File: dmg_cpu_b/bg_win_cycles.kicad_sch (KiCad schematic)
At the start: 68 parts

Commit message: Fixes based on review. + various other edits.
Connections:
- net CLK2: now also LEBO.1
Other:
- moved on the sheet: LYRY, MOCE
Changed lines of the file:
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@@
     (comment 1 "https://github.com/msinger/dmg-schematics")
   )
-  (junction (at 104.14 89.535) (diameter 0) (color 0 0 0 0)
+  (junction (at 104.14 85.725) (diameter 0) (color 0 0 0 0)
   )
   (junction (at 48.26 54.61) (diameter 0) (color 0 0 0 0)
@@
   (junction (at 153.035 253.365) (diameter 0) (color 0 0 0 0)
   )
+  (junction (at 81.28 71.755) (diameter 0) (color 0 0 0 0)
+  )
   (junction (at 183.515 255.905) (diameter 0) (color 0 0 0 0)
   )
@@
   (junction (at 76.2 76.835) (diameter 0) (color 0 0 0 0)
   )
-  (junction (at 48.26 89.535) (diameter 0) (color 0 0 0 0)
+  (junction (at 130.175 85.725) (diameter 0) (color 0 0 0 0)
   )
   (junction (at 262.89 150.495) (diameter 0) (color 0 0 0 0)
@@
   (junction (at 168.91 111.125) (diameter 0) (color 0 0 0 0)
   )
+  (junction (at 48.26 85.725) (diameter 0) (color 0 0 0 0)
+  )
   (junction (at 188.595 231.14) (diameter 0) (color 0 0 0 0)
   )
@@
   )
   (junction (at 297.815 227.33) (diameter 0) (color 0 0 0 0)
-  )
-  (junction (at 78.74 71.755) (diameter 0) (color 0 0 0 0)
   )
   (junction (at 343.535 214.63) (diameter 0) (color 0 0 0 0)
@@
     (stroke (width 0) (type default) (color 0 0 0 0))
   )
-  (wire (pts (xy 73.66 71.755) (xy 78.74 71.755))
+  (wire (pts (xy 73.66 71.755) (xy 81.28 71.755))
     (stroke (width 0) (type default) (color 0 0 0 0))
   )
@@
     (stroke (width 0) (type default) (color 0 0 0 0))
   )
+  (wire (pts (xy 130.175 85.725) (xy 130.175 89.535))
+    (stroke (width 0) (type default) (color 0 0 0 0))
+  )
   (wire (pts (xy 300.355 217.17) (xy 300.355 212.09))
     (stroke (width 0) (type default) (color 0 0 0 0))
@@
     (stroke (width 0) (type default) (color 0 0 0 0))
   )
-  (wire (pts (xy 27.94 95.25) (xy 104.14 95.25))
+  (wire (pts (xy 27.94 92.075) (xy 104.14 92.075))
     (stroke (width 0) (type default) (color 0 0 0 0))
   )
@@
     (stroke (width 0) (type default) (color 0 0 0 0))
   )
-  (wire (pts (xy 101.6 89.535) (xy 104.14 89.535))
+  (wire (pts (xy 101.6 85.725) (xy 104.14 85.725))
     (stroke (width 0) (type default) (color 0 0 0 0))
   )
@@
     (stroke (width 0) (type default) (color 0 0 0 0))
   )
-  (wire (pts (xy 83.82 32.385) (xy 83.82 86.995))
-    (stroke (width 0) (type default) (color 0 0 0 0))
-  )
-  (wire (pts (xy 48.26 74.295) (xy 48.26 89.535))
+  (wire (pts (xy 83.82 32.385) (xy 83.82 83.185))
+    (stroke (width 0) (type default) (color 0 0 0 0))
+  )
+  (wire (pts (xy 48.26 74.295) (xy 48.26 85.725))
     (stroke (width 0) (type default) (color 0 0 0 0))
   )
@@
     (stroke (width 0) (type default) (color 0 0 0 0))
   )
-  (wire (pts (xy 48.26 89.535) (xy 86.36 89.535))
+  (wire (pts (xy 48.26 85.725) (xy 86.36 85.725))
     (stroke (width 0) (type default) (color 0 0 0 0))
   )
@@
     (stroke (width 0) (type default) (color 0 0 0 0))
   )
-  (wire (pts (xy 83.82 86.995) (xy 86.36 86.995))
+  (wire (pts (xy 83.82 83.185) (xy 86.36 83.185))
     (stroke (width 0) (type default) (color 0 0 0 0))
   )
@@
     (stroke (width 0) (type default) (color 0 0 0 0))
   )
-  (wire (pts (xy 78.74 71.755) (xy 78.74 92.075))
+  (wire (pts (xy 81.28 71.755) (xy 81.28 88.265))
     (stroke (width 0) (type default) (color 0 0 0 0))
   )
@@
     (stroke (width 0) (type default) (color 0 0 0 0))
   )
-  (wire (pts (xy 27.94 74.295) (xy 27.94 95.25))
+  (wire (pts (xy 27.94 74.295) (xy 27.94 92.075))
     (stroke (width 0) (type default) (color 0 0 0 0))
   )
@@
     (stroke (width 0) (type default) (color 0 0 0 0))
   )
+  (wire (pts (xy 81.28 71.755) (xy 94.615 71.755))
+    (stroke (width 0) (type default) (color 0 0 0 0))
+  )
   (wire (pts (xy 302.26 133.985) (xy 304.8 133.985))
     (stroke (width 0) (type default) (color 0 0 0 0))
@@
     (stroke (width 0) (type default) (color 0 0 0 0))
   )
-  (wire (pts (xy 104.14 89.535) (xy 106.68 89.535))
+  (wire (pts (xy 104.14 85.725) (xy 106.68 85.725))
     (stroke (width 0) (type default) (color 0 0 0 0))
   )
@@
     (stroke (width 0) (type default) (color 0 0 0 0))
   )
-  (wire (pts (xy 130.175 80.01) (xy 130.175 89.535))
+  (wire (pts (xy 130.175 80.01) (xy 130.175 85.725))
     (stroke (width 0) (type default) (color 0 0 0 0))
   )
@@
     (stroke (width 0) (type default) (color 0 0 0 0))
   )
-  (wire (pts (xy 130.175 89.535) (xy 119.38 89.535))
+  (wire (pts (xy 130.175 85.725) (xy 119.38 85.725))
     (stroke (width 0) (type default) (color 0 0 0 0))
   )
@@
     (stroke (width 0) (type default) (color 0 0 0 0))
   )
-  (wire (pts (xy 104.14 89.535) (xy 104.14 95.25))
+  (wire (pts (xy 104.14 85.725) (xy 104.14 92.075))
     (stroke (width 0) (type default) (color 0 0 0 0))
   )
@@
     (stroke (width 0) (type default) (color 0 0 0 0))
   )
-  (wire (pts (xy 78.74 71.755) (xy 94.615 71.755))
-    (stroke (width 0) (type default) (color 0 0 0 0))
-  )
   (wire (pts (xy 53.34 74.295) (xy 48.26 74.295))
     (stroke (width 0) (type default) (color 0 0 0 0))
@@
     (stroke (width 0) (type default) (color 0 0 0 0))
   )
-  (wire (pts (xy 48.26 89.535) (xy 48.26 97.155))
+  (wire (pts (xy 48.26 85.725) (xy 48.26 97.155))
     (stroke (width 0) (type default) (color 0 0 0 0))
   )
@@
     (stroke (width 0) (type default) (color 0 0 0 0))
   )
-  (wire (pts (xy 78.74 92.075) (xy 86.36 92.075))
+  (wire (pts (xy 81.28 88.265) (xy 86.36 88.265))
     (stroke (width 0) (type default) (color 0 0 0 0))
   )
@@
   )
   (text "HORIZONTAL SYNC" (at 378.46 162.56 0)
+    (effects (font (size 1.27 1.27)) (justify left bottom))
+  )
+  (label "CLK2" (at 25.4 69.215 0)
     (effects (font (size 1.27 1.27)) (justify left bottom))
   )
@@
     (pin "2")
   )
-  (symbol (lib_id "DMG_CPU_Cells:NAND_3") (at 93.98 89.535 0) (unit 1)
-    (in_bom yes) (on_board yes) (fields_autoplaced)
-    (property "Reference" "MOCE" (id 0) (at 93.98 82.0252 0))
-    (property "Value" "NAND_3" (id 1) (at 93.98 84.5621 0))
-    (property "Footprint" "" (id 2) (at 93.98 89.535 0)
-      (effects (font (size 1.27 1.27)) hide)
-    )
-    (property "Datasheet" "http://iceboy.a-singer.de/doc/dmg_cells.html#nand3" (id 3) (at 93.98 97.155 0)
+  (symbol (lib_id "DMG_CPU_Cells:NAND_3") (at 93.98 85.725 0) (unit 1)
+    (in_bom yes) (on_board yes) (fields_autoplaced)
+    (property "Reference" "MOCE" (id 0) (at 93.98 78.2152 0))
+    (property "Value" "NAND_3" (id 1) (at 93.98 80.7521 0))
+    (property "Footprint" "" (id 2) (at 93.98 85.725 0)
+      (effects (font (size 1.27 1.27)) hide)
+    )
+    (property "Datasheet" "http://iceboy.a-singer.de/doc/dmg_cells.html#nand3" (id 3) (at 93.98 93.345 0)
       (effects (font (size 1.27 1.27)) hide)
     )
@@
     (pin "4")
   )
-  (symbol (lib_id "DMG_CPU_Cells:INVERTER_A") (at 113.03 89.535 0) (unit 1)
-    (in_bom yes) (on_board yes) (fields_autoplaced)
-    (property "Reference" "LYRY" (id 0) (at 113.03 82.0252 0))
-    (property "Value" "INVERTER_A" (id 1) (at 113.03 84.5621 0))
-    (property "Footprint" "" (id 2) (at 110.49 89.535 0)
-      (effects (font (size 1.27 1.27)) hide)
-    )
-    (property "Datasheet" "http://iceboy.a-singer.de/doc/dmg_cells.html#inv_a" (id 3) (at 114.3 97.155 0)
-      (effects (font (size 1.27 1.27)) hide)
-    )
+  (symbol (lib_id "DMG_CPU_Cells:INVERTER_A") (at 113.03 85.725 0) (unit 1)
+    (in_bom yes) (on_board yes) (fields_autoplaced)
+    (property "Reference" "LYRY" (id 0) (at 113.03 78.2152 0))
+    (property "Value" "INVERTER_A" (id 1) (at 113.03 80.7521 0))
+    (property "Footprint" "" (id 2) (at 110.49 85.725 0)
+      (effects (font (size 1.27 1.27)) hide)
+    )
+    (property "Datasheet" "http://iceboy.a-singer.de/doc/dmg_cells.html#inv_a" (id 3) (at 114.3 93.345 0)
+      (effects (font (size 1.27 1.27)) hide)
+    )

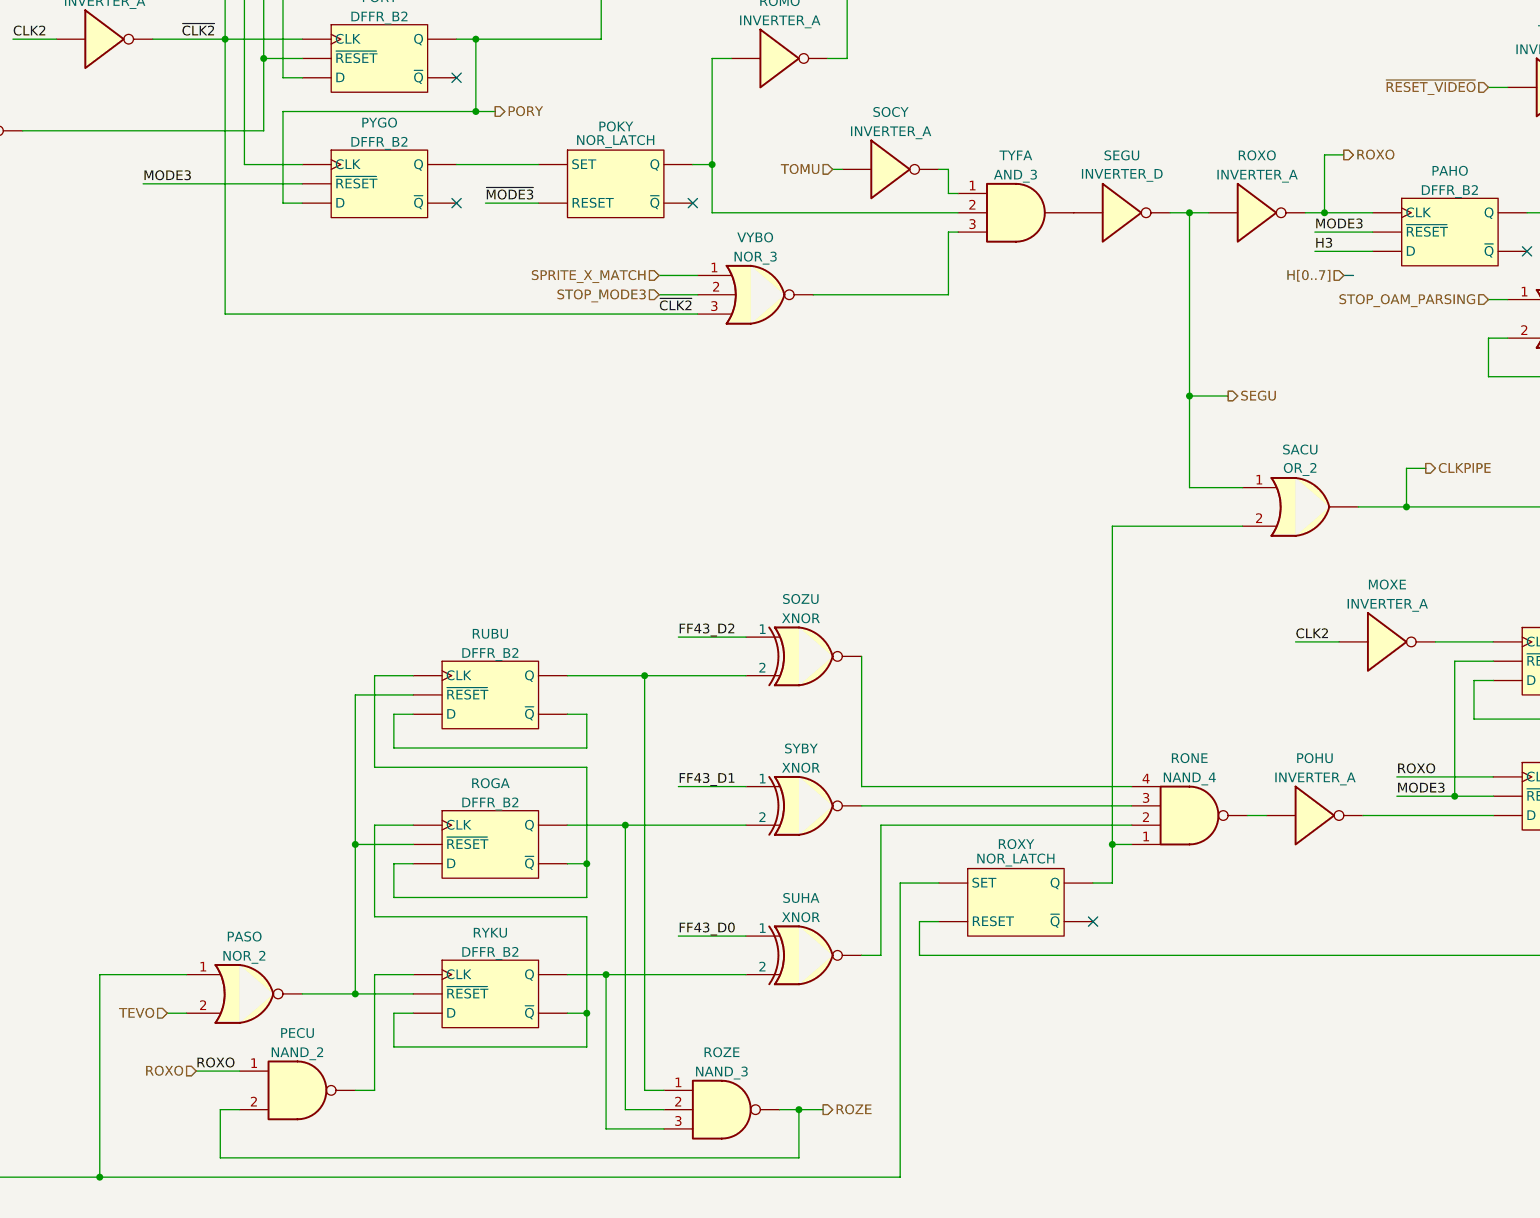
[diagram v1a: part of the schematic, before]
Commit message: Changes made based on review. PPU hierarchcal sheet work started.
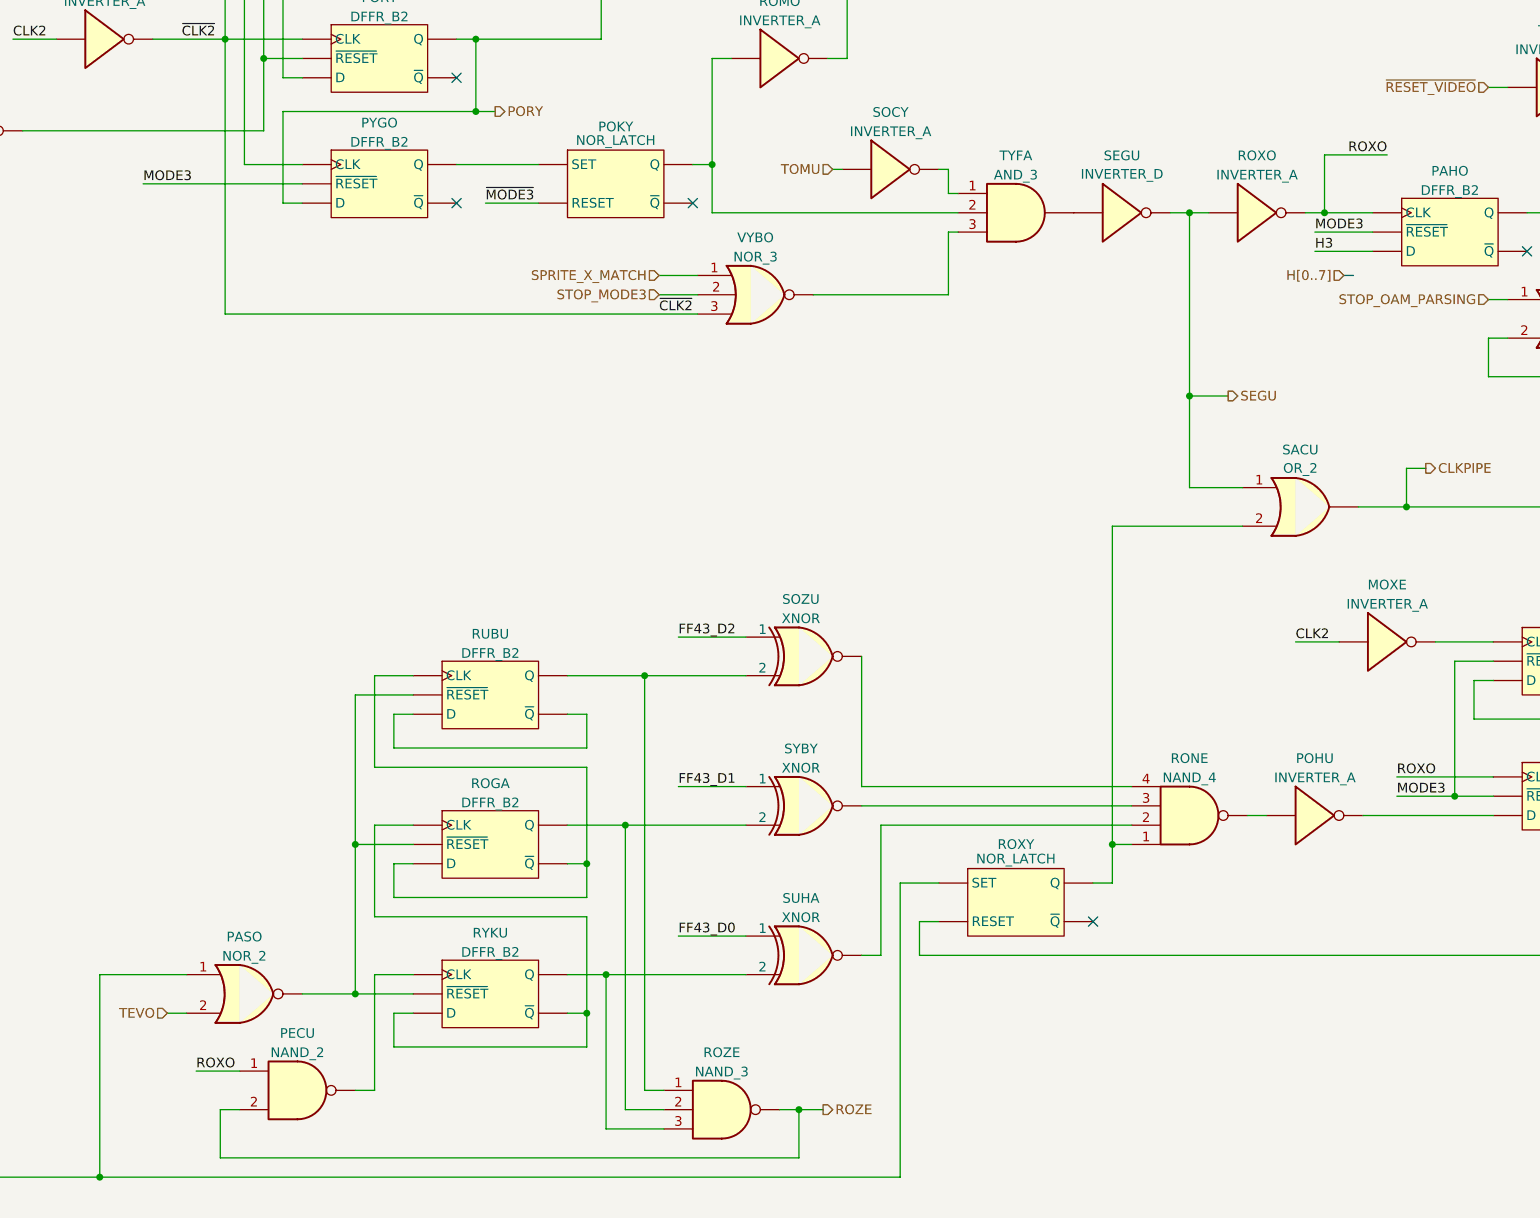
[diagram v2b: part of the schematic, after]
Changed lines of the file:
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@@
     (stroke (width 0) (type default) (color 0 0 0 0))
   )
-  (wire (pts (xy 280.67 142.875) (xy 283.21 142.875))
+  (wire (pts (xy 280.67 142.875) (xy 288.925 142.875))
     (stroke (width 0) (type default) (color 0 0 0 0))
   )
@@
     (effects (font (size 1.27 1.27)) (justify left bottom))
   )
+  (label "ROXO" (at 288.925 142.875 180)
+    (effects (font (size 1.27 1.27)) (justify right bottom))
+  )
   (label "ROXO" (at 290.195 224.79 0)
     (effects (font (size 1.27 1.27)) (justify left bottom))
@@
     (effects (font (size 1.27 1.27)) (justify left))
   )
-  (hierarchical_label "ROXO" (shape input) (at 132.08 263.525 180)
-    (effects (font (size 1.27 1.27)) (justify right))
-  )
   (hierarchical_label "MOFU" (shape output) (at 207.01 61.595 0)
     (effects (font (size 1.27 1.27)) (justify left))
@@
     (effects (font (size 1.27 1.27)) (justify left))
   )
-  (hierarchical_label "ROXO" (shape output) (at 283.21 142.875 0)
-    (effects (font (size 1.27 1.27)) (justify left))
-  )

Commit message: PPU hierarchical page progress. Elements moved out of window sheet to be includes in BG and WIN cycles sheet
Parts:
- added MEHE, NOCU, NYFO, ROCO, SYLO, TOMU, XACO, XAHY: INVERTER_A, symbol DMG_CPU_Cells:INVERTER_A
- added MOSU, PORE, SUZU: INVERTER_B, symbol DMG_CPU_Cells:INVERTER_B
- added NOPA, NUNU, PYCO, RENE, RYFA, SOVY: DFFR_B2, symbol DMG_CPU_Cells:DFFR_B2
- added NUNY, VETU: AND_2, symbol DMG_CPU_Cells:AND_2
- added NYXU, RYDY: NOR_3, symbol DMG_CPU_Cells:NOR_3
- added PANY, PUKU, SEKO: NOR_2, symbol DMG_CPU_Cells:NOR_2
- added PYNU: NOR_LATCH, symbol DMG_CPU_Cells:NOR_LATCH
- added TEVO: OR_3, symbol DMG_CPU_Cells:OR_3
- added TUXY: NAND_2, symbol DMG_CPU_Cells:NAND_2
- added XOFO: NAND_3, symbol DMG_CPU_Cells:NAND_3
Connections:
- net MODE3: now also RENE.2 (~{RESET}), RENE.4 (~{RESET}), RYFA.2 (~{RESET}), RYFA.4 (~{RESET})
- net PORY: now also RYDY.2
- net ROZE: now also PANY.1
- net SEGU: now also ROCO.1, RYFA.1 (CLK)
- net STOP_OAM_PARSING: now also NYXU.1
- net TAVE: now also TEVO.3
- net TEVO: now also NYXU.3, TEVO.4, VETU.1
- net TOMU: now also TOMU.2
- net ~{RESET_VIDEO}: now also NOPA.2 (~{RESET}), NOPA.4 (~{RESET}), NUNU.2 (~{RESET}), NUNU.4 (~{RESET}), PYCO.2 (~{RESET}), PYCO.4 (~{RESET}), SOVY.2 (~{RESET}), SOVY.4 (~{RESET}), XOFO.3
- net CLK2 renamed ~{PPU_4MHz}
- net ~{PPU_4MHz}: now also MEHE.1, NOPA.1 (CLK), RENE.1 (CLK), SOVY.1 (CLK)
- net MOFU renamed ~{CLK_BG_BP_B}
- net NYDY renamed ~{LATCH_BG_BP_A}
- net NYXU renamed ~{BG_CY_RST}
- net ~{BG_CY_RST}: now also NYXU.4
- net WIN_START_PULSE2: no longer names the net of NAFY.2
- net WIN_START_PULSE2: now also MOSU.2, NYXU.2
- new net: PANY.3, RYFA.3 (D)
- new net: NOCU.1, NOPA.3 (D), NUNY.1, PYNU.3 (Q)
- new net: NOPA.5 (~{Q}), NUNY.2
- new net: NUNU.6 (Q), PYNU.1 (SET)
- new net: PYNU.4 (RESET), XACO.1, XOFO.4
- new net: XAHY.2, XOFO.2
- new net: NOCU.2, PORE.1
- new net: RENE.3 (D), RYFA.6 (Q)
- new net: RENE.6 (Q), SEKO.2
- new net: MEHE.2, NUNU.1 (CLK)
- new net: NUNU.3 (D), PYCO.6 (Q)
- new net: RYFA.5 (~{Q}), SEKO.1
- new net: SEKO.3, TEVO.1
- new net: PUKU.3, RYDY.1
- new net: PUKU.2, RYDY.4, SOVY.3 (D), SYLO.1
- new net: SOVY.6 (Q), TUXY.1
- new net: SUZU.1, TUXY.3
- new net: SUZU.2, TEVO.2
- new net: PYCO.1 (CLK), ROCO.2
- new net: MOSU.1, NYFO.2
- new net: SYLO.2, TOMU.1, TUXY.2
- new net ATEJ: XAHY.1
- new net FF40_D5: XOFO.1
- new net IN_WINDOW: PORE.2, VETU.2
- new net RESET_VIDEO2: RYDY.3
- new net WIN_START_PULSE: NUNY.3, NYFO.1, PUKU.1
- new net WXY_MATCH: PANY.2, PYCO.3 (D)
- new net WX_CLK: VETU.3
- new net ~{WX_RST}: XACO.2
- no-connect marks 11 -> 17
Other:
- note added: "BG/WIN Cycle counter"
- note added: "TAVE resets the cycle counter at cycle 5 only once at the start of a new rendering line. PORY will reset the counter when Window has started at cycle 5 too. ROZE will reset the counter at cycle 7 in other cases."
- note added: "{signal: [ {name: '/PPU_4MHz', wave: '101010101010101010101010101010101'}, {name: 'MODE3', wave: '0...1............................'}, {name: '/BG_CY_RST', wave: '0...1..........01..............01'}, {name: 'LAXU.Q', wave: '0....1.0.1.0.1.0.1.0.1.0.1.....0.'}, {name: 'MESU.Q', wave: '0......1...0.......1...0.........'}, {name: 'NYVA.Q', wave: '0..........1...0.......1.......0.'}, {name: 'LYRY', w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"
- moved on the sheet: CP, LAXE, LAXU, LEBO, LENA, LOBY, LONY, LOVY, LURY, LUSU, LYRY, LYZU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

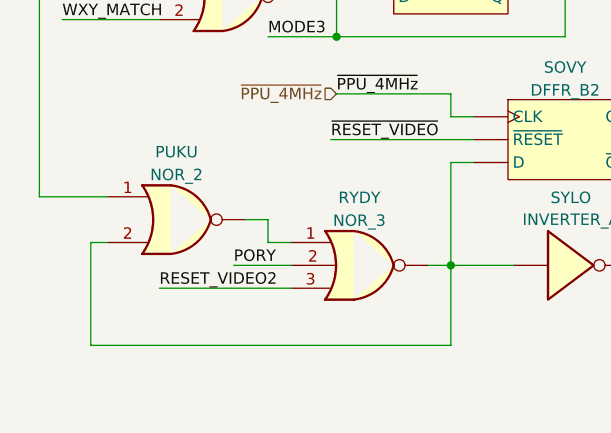
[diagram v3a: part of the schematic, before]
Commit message: All connections between sheet are complete. Can still do with a good tidy up.
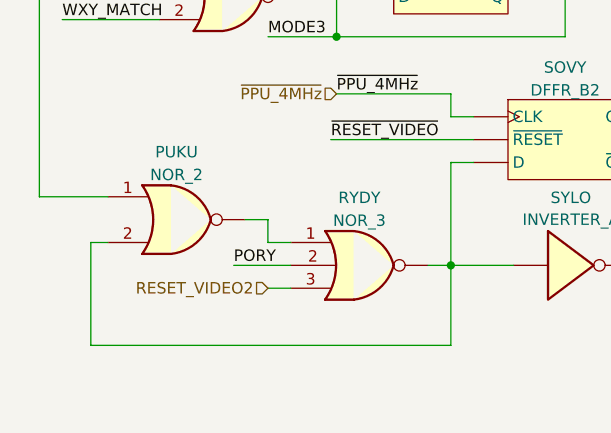
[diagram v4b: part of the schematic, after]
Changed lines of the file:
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@@
     (stroke (width 0) (type default) (color 0 0 0 0))
   )
-  (wire (pts (xy 27.305 267.335) (xy 41.91 267.335))
+  (wire (pts (xy 39.37 267.335) (xy 41.91 267.335))
     (stroke (width 0) (type default) (color 0 0 0 0))
   )
@@
     (effects (font (size 1.27 1.27)) (justify left bottom))
   )
-  (label "RESET_VIDEO2" (at 27.305 267.335 0)
-    (effects (font (size 1.27 1.27)) (justify left bottom))
-  )
   (label "~{BG_CY_RST}" (at 168.275 200.66 180)
     (effects (font (size 1.27 1.27)) (justify right bottom))
@@
     (effects (font (size 1.27 1.27)) (justify left))
   )
+  (hierarchical_label "RESET_VIDEO2" (shape input) (at 39.37 267.335 180)
+    (effects (font (size 1.27 1.27)) (justify right))
+  )
   (hierarchical_label "~{WX_RST}" (shape output) (at 109.22 151.765 0)
